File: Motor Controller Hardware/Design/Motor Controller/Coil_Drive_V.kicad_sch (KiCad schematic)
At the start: 15 parts, among them Q7 NMOS, Q8 NMOS, U10 AD8418

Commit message: a:
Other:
- title: (none) -> HyperDrive Motor Controller
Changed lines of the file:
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@@
 	(paper "A4")
 	(title_block
-		(rev "1")
+		(title "HyperDrive Motor Controller")
+		(rev "Mk. 1")
 		(company "University of Alberta EcoCar Team")
 	)

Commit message: A
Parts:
- added C91: 1n, symbol Device:C
- added D13, D14: D_Zener, symbol Device:D_Zener
- added R43, R44: 10k, symbol Device:R
- C43: value 100n -> 1n
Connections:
- net GND: now also C91.2, D13.2 (A), D14.2 (A), R43.1, R44.1
- net V_{SENSE, V, 2}: now also C91.1
- net at D5.2 (A), Q8.2 (G), R20.2: now also D14.1 (K), R44.2
- net at D4.2 (A), Q7.2 (G), R19.2: now also D13.1 (K), R43.2
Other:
- moved on the sheet: C42, C43, C44, C45, C46, Q7, Q8, R21, R22, U10

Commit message: Almost done power delivery
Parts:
- renumbered C41 to C79, C42 to C80, C43 to C81, C44 to C82, C91 to C83, C45 to C84, C46 to C85, D4 to D12, D5 to D13, D13 to D14, D14 to D15, Q7 to Q6, Q8 to Q7, R19 to R38, R20 to R39, R43 to R40, R44 to R41, R21 to R42, R22 to R43, U10 to U13
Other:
- moved on the sheet: C84, C85, R43, U13

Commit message: Added foot prints and started layout
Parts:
- C79, C81, C83, C84, C85: footprint (none) -> Capacitor_SMD:C_0603_1608Metric
- C80: footprint (none) -> Capacitor_SMD:C_0805_2012Metric
- R38, R39, R40, R41, R42, R43: footprint (none) -> Resistor_SMD:R_0603_1608Metric
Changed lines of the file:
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@@
 			)
 		)
-		(property "Footprint" ""
+		(property "Footprint" "Resistor_SMD:R_0603_1608Metric"
 			(at 182.88 102.108 90)
 			(effects
@@
 			)
 		)
-		(property "Footprint" ""
+		(property "Footprint" "Resistor_SMD:R_0603_1608Metric"
 			(at 118.11 124.968 90)
 			(effects
@@
 			)
 		)
-		(property "Footprint" ""
+		(property "Footprint" "Resistor_SMD:R_0603_1608Metric"
 			(at 118.11 79.248 90)
 			(effects
@@
 			)
 		)
-		(property "Footprint" ""
+		(property "Footprint" "Resistor_SMD:R_0603_1608Metric"
 			(at 133.858 83.82 90)
 			(effects
@@
 			)
 		)
-		(property "Footprint" ""
+		(property "Footprint" "Resistor_SMD:R_0603_1608Metric"
 			(at 259.08 102.108 90)
 			(effects
@@
 			)
 		)
-		(property "Footprint" ""
+		(property "Footprint" "Capacitor_SMD:C_0805_2012Metric"
 			(at 168.6052 74.93 0)
 			(effects
@@
 			)
 		)
-		(property "Footprint" ""
+		(property "Footprint" "Capacitor_SMD:C_0603_1608Metric"
 			(at 114.3 101.2952 0)
 			(effects
@@
 			)
 		)
-		(property "Footprint" ""
+		(property "Footprint" "Capacitor_SMD:C_0603_1608Metric"
 			(at 268.9352 110.49 0)
 			(effects
@@
 			)
 		)
-		(property "Footprint" ""
+		(property "Footprint" "Resistor_SMD:R_0603_1608Metric"
 			(at 133.858 129.54 90)
 			(effects
@@
 			)
 		)
-		(property "Footprint" ""
+		(property "Footprint" "Capacitor_SMD:C_0603_1608Metric"
 			(at 173.6852 113.03 0)
 			(effects
@@
 			)
 		)
-		(property "Footprint" ""
+		(property "Footprint" "Capacitor_SMD:C_0603_1608Metric"
 			(at 219.4052 110.49 0)
 			(effects
@@
 			)
 		)
-		(property "Footprint" ""
+		(property "Footprint" "Capacitor_SMD:C_0603_1608Metric"
 			(at 194.0052 113.03 0)
 			(effects

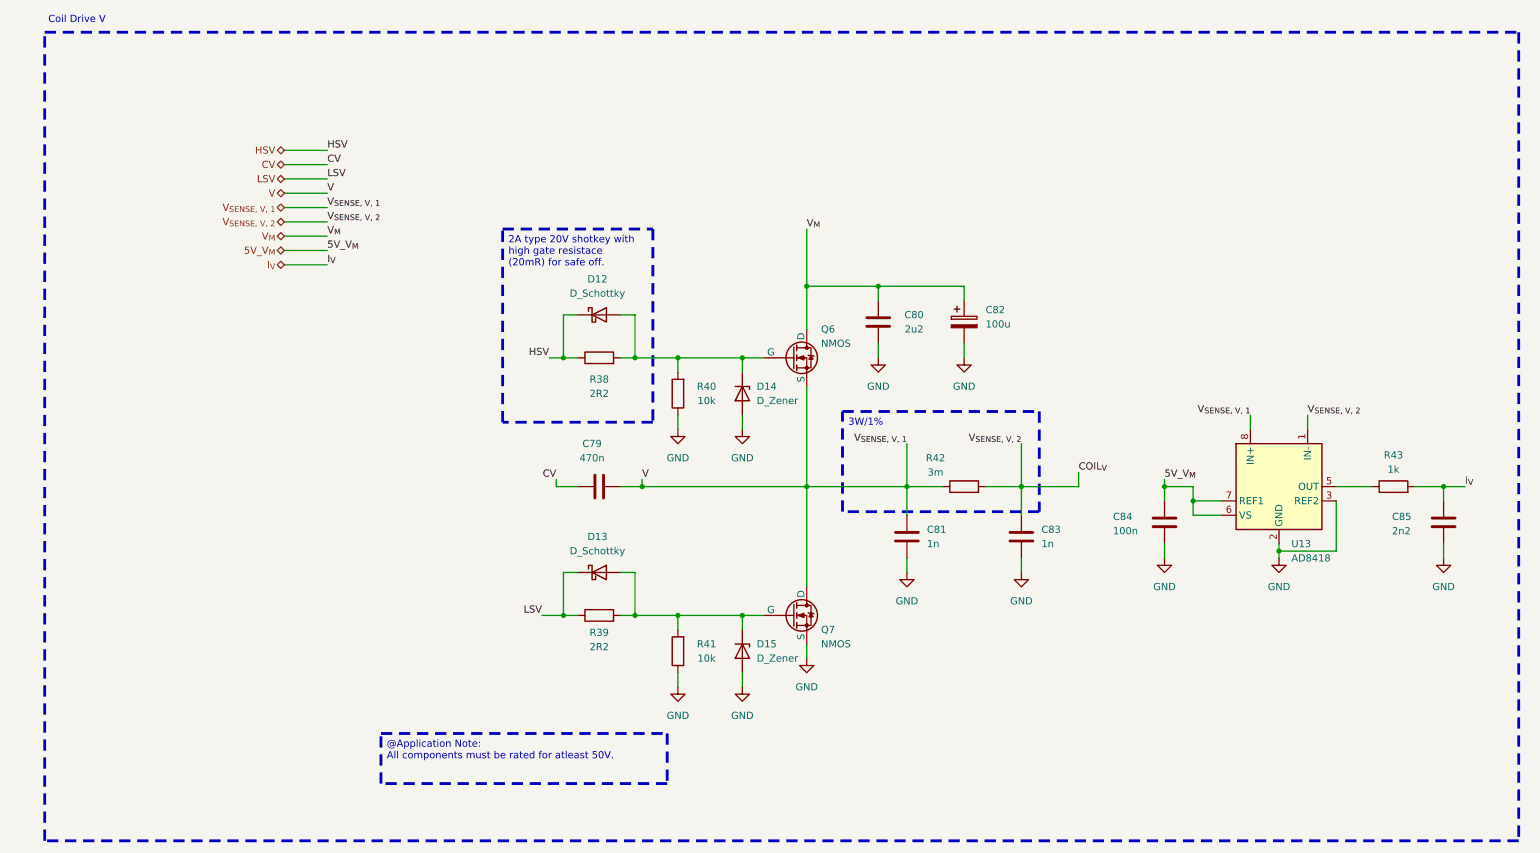
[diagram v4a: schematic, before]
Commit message: Will now just do rev 1 as Silicon mosfets and rev 2 will be gan
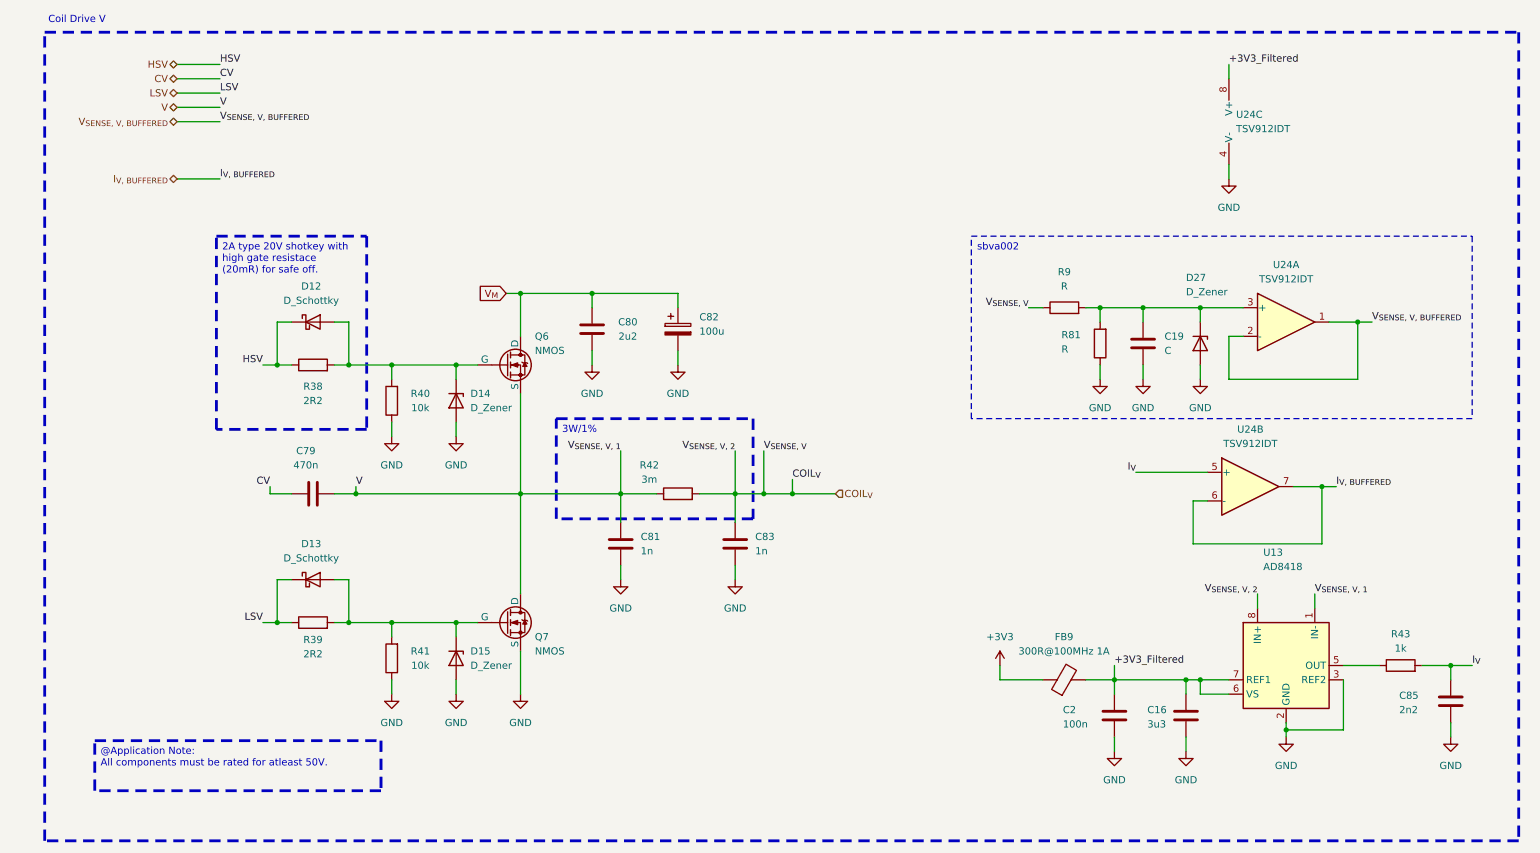
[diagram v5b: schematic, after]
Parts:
- removed C84: 100n, Capacitor_SMD:C_0603_1608Metric, symbol Device:C
- added C16: 3u3, Capacitor_SMD:C_0603_1608Metric, symbol Device:C
- added C19: C, Capacitor_SMD:C_0603_1608Metric, symbol Device:C
- added C2: 100n, Capacitor_SMD:C_0603_1608Metric, symbol Device:C
- added D27: D_Zener, symbol Device:D_Zener
- added FB9: 300R@100MHz 1A, Inductor_SMD:L_0603_1608Metric, symbol Device:FerriteBead
- added R81, R9: R, Resistor_SMD:R_0603_1608Metric, symbol Device:R
- added U24: TSV912IDT, Package_SO:SOIC-8_3.9x4.9mm_P1.27mm, symbol Amplifier_Operational:TSV912IDT
- U13: footprint (none) -> Package_SO:MSOP-8_3x3mm_P0.65mm; DK# (none) -> 505-AD8418BRMZ-RLCT-ND
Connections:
- net GND: now also C16.2, C19.2, C2.2, D27.2 (A), R81.1, U24.4 (V-)
- net I_{V}: now also U24.5 (+)
- net V: now also U13.1 (IN-); no longer U13.8 (IN+)
- net 5V_V_{M} renamed +3V3_Filtered
- net +3V3_Filtered: now also C16.1, C2.1, FB9.2, U24.8 (V+)
- net V_{SENSE, V, 2} renamed COIL_{V}
- net COIL_{V}: now also U13.8 (IN+), R9.1; no longer U13.1 (IN-)
- new net: C19.1, D27.1 (K), R81.2, R9.2, U24.3 (+)
- new net +3V3: FB9.1
- new net I_{V, BUFFERED}: U24.6 (-), U24.7
- new net V_{SENSE, V, BUFFERED}: U24.1, U24.2 (-)
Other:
- moved on the sheet: C79, C80, C81, C82, C83, C85, D12, D13, D14, D15, Q6, Q7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

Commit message: A
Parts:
- added C146: C, Capacitor_SMD:C_0603_1608Metric, symbol Device:C
- added C149: 100n, Capacitor_SMD:C_0603_1608Metric, symbol Device:C
- added D31: D_Zener, symbol Device:D_Zener
- added R94, R95: R, Resistor_SMD:R_0603_1608Metric, symbol Device:R
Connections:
- net +3V3_Filtered: no longer U13.7 (REF1)
- net COIL_{V}: now also U13.1 (IN-); no longer U13.8 (IN+)
- net GND: now also C146.2, C149.2, D31.2 (A), R95.1; no longer U13.3 (REF2)
- net I_{V}: now also R94.1; no longer U24.5 (+)
- net V: now also U13.8 (IN+); no longer U13.1 (IN-)
- new net: C146.1, D31.1 (K), R94.2, R95.2, U24.5 (+)
- new net VREF_2.5: C149.1, U13.3 (REF2), U13.7 (REF1)
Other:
- moved on the sheet: C16, C2, FB9

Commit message: A
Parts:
- added C155: 100n, Capacitor_SMD:C_0603_1608Metric, symbol Device:C
- R81: value R -> 10k
- R9: value R -> 147k
- R94: value R -> 5k
- R95: value R -> 9k76
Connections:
- net +3V3_Filtered: now also C155.1
- net GND: now also C155.2

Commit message: A
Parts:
- C82: footprint (none) -> ecocad:CHEMI-KE0; DK# (none) -> 565-2511-1-ND
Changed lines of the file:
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@@
 			)
 		)
-		(property "Footprint" ""
+		(property "Footprint" "ecocad:CHEMI-KE0"
 			(at 133.0452 76.2 0)
 			(effects
@@
 			(at 132.08 72.39 0)
 			(effects
+				(font
+					(size 1.27 1.27)
+				)
+				(hide yes)
+			)
+		)
+		(property "DK#" "565-2511-1-ND"
+			(at 132.08 72.39 0)
+			(effects
